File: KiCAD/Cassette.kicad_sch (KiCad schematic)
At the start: 46 parts, among them J3 Front View, K1 Relay_SPST-NO

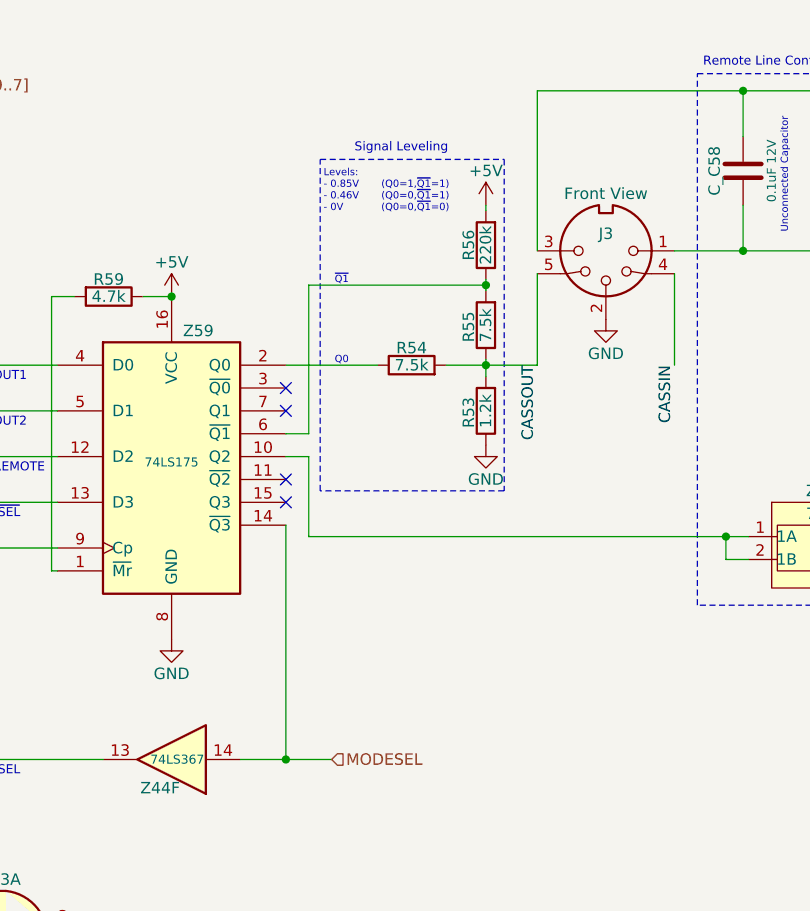
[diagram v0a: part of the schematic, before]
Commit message: Cleanup, Changelog added & Curiosities photos
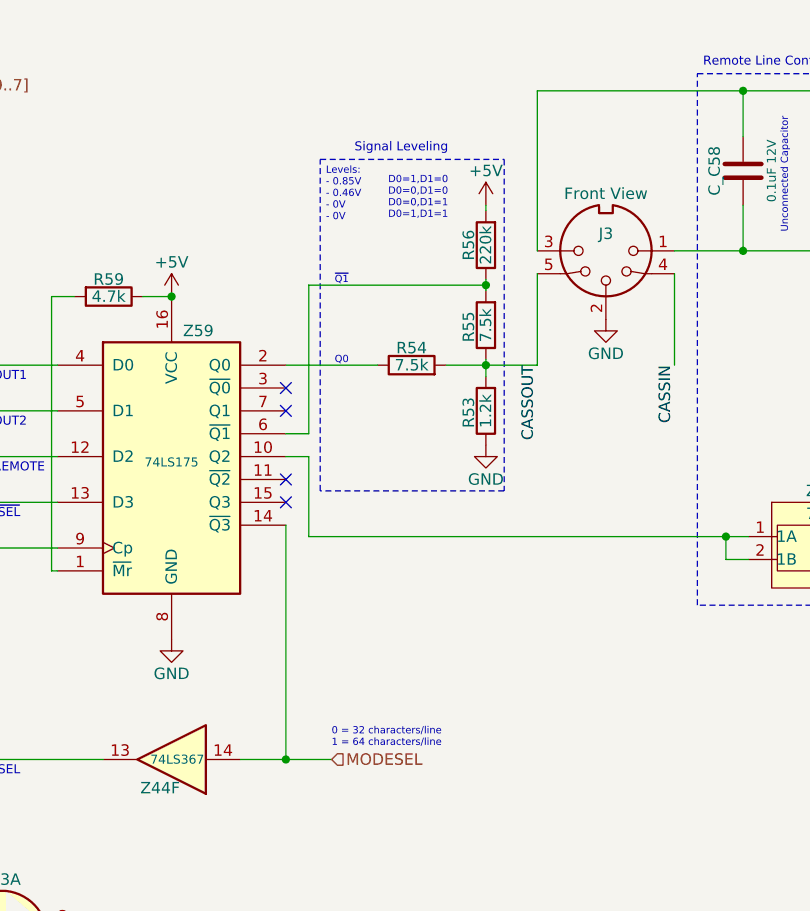
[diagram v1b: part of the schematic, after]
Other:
- note added: "0 = 32 characters/line 1 = 64 characters/line"
- note added: "D0=1,D1=0 D0=0,D1=0 D0=0,D1=1 D0=1,D1=1"
- note added: "Levels: - 0.85V - 0.46V - 0V - 0V"
- note removed: "(Q0=1,~{Q1}=1) (Q0=0,~{Q1}=1) (Q0=0,~{Q1}=0)"
- note removed: "Levels: - 0.85V - 0.46V - 0V"
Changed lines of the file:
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@@
     (effects (font (size 1 1)) (justify left bottom))
+  )
+  (text "0 = 32 characters/line\n1 = 64 characters/line\n" (at 182.245 158.75 0)
+    (effects (font (size 0.8 0.8)) (justify left bottom))
   )
   (text "Full-wave\nRectifier" (at 106.68 42.545 0)
@@
     (effects (font (size 0.8 0.8)) (justify right bottom))
   )
-  (text "Levels:\n- 0.85V\n- 0.46V\n- 0V" (at 181.356 99.314 0)
+  (text "Levels:\n- 0.85V\n- 0.46V\n- 0V\n- 0V" (at 181.61 100.33 0)
     (effects (font (size 0.8 0.8)) (justify left bottom))
   )
@@
     (effects (font (size 0.8 0.8)) (justify left bottom))
   )
-  (text "(Q0=1,~{Q1}=1)\n(Q0=0,~{Q1}=1)\n(Q0=0,~{Q1}=0)" (at 195.326 99.314 0)
+  (text "D0=1,D1=0\nD0=0,D1=0\nD0=0,D1=1\nD0=1,D1=1" (at 195.199 100.076 0)
     (effects (font (size 0.8 0.8)) (justify right bottom))
   )

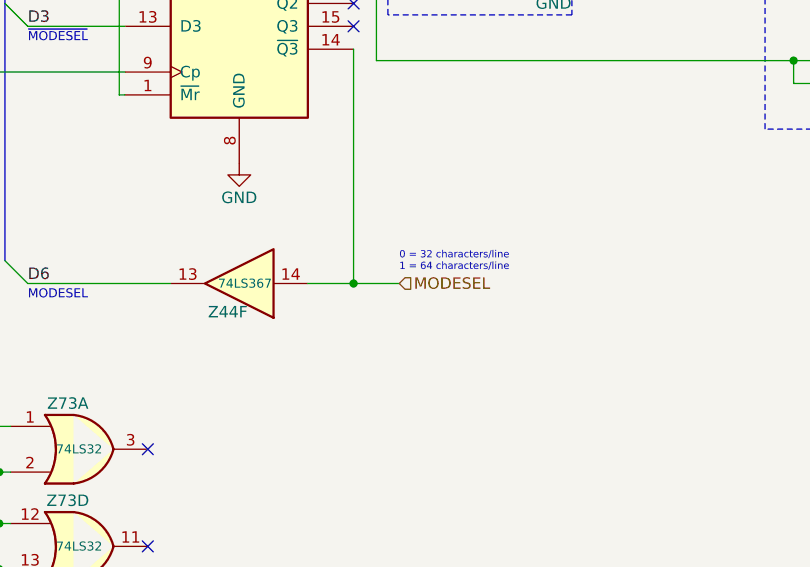
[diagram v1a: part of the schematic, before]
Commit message: Update schematics (correct page flow) and add alternative to Q4 in BOM
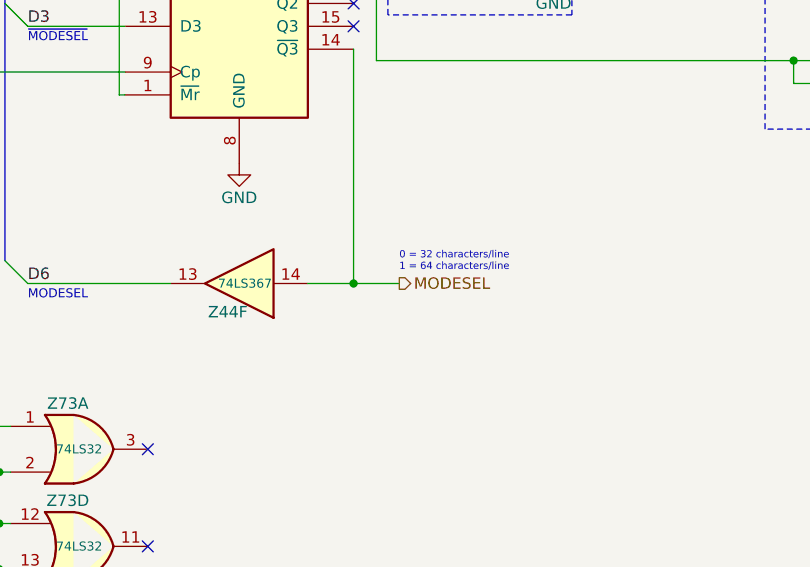
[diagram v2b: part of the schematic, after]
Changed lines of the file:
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@@
     (effects (font (size 1.27 1.27)) (justify right))
   )
-  (hierarchical_label "MODESEL" (shape input) (at 182.245 160.02 0) (fields_autoplaced)
+  (hierarchical_label "MODESEL" (shape output) (at 182.245 160.02 0) (fields_autoplaced)
     (effects (font (size 1.27 1.27)) (justify left))
   )

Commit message: Updated revision to Rev C
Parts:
- gave numbers to parts that had none: 1
- renumbered Z73 to Z25
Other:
- title: TRS-80 Model I G -> TRS-80 Model I Rev G
